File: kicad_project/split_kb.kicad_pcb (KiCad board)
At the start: 2 copper layers, 122 parts, among them J1 Conn_01x03_Pin, J2 Conn_01x04_Socket, J3 4P4C, SW1 B3S-1002

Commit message: Add gitignore (again)
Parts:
- moved H3 135.3 mm to (232.8, 23.8)
- moved J2 62.2 mm to (75.0, 42.7)
- moved J1 35.5 mm to (75.0, 60.5), turned to 180 degrees
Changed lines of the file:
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@@
 	(footprint "MountingHole:MountingHole_3mm_Pad_Via"
 		(layer "F.Cu")
-		(at 216.6 158.05)
+		(at 232.75 23.75)
 		(descr "Mounting Hole 3mm")
 		(tags "mounting hole 3mm")
@@
 	(footprint "Connector_PinHeader_2.54mm:PinHeader_1x04_P2.54mm_Vertical"
 		(layer "F.Cu")
-		(at 26.6 81.7)
+		(at 75.05 42.73)
 		(descr "Through hole straight pin header, 1x04, 2.54mm pitch, single row")
 		(tags "Through hole pin header THT 1x04 2.54mm single row")
@@
 	(footprint "Connector_PinHeader_2.54mm:PinHeader_1x03_P2.54mm_Vertical"
 		(layer "F.Cu")
-		(at 61.769996 93.45 90)
+		(at 75.05 60.49 180)
 		(descr "Through hole straight pin header, 1x03, 2.54mm pitch, single row")
 		(tags "Through hole pin header THT 1x03 2.54mm single row")
 		(property "Reference" "J1"
-			(at 0 -2.33 -90)
+			(at 0 -2.33 180)
 			(layer "F.SilkS")
 			(effects
@@
 		)
 		(property "Value" "Conn_01x03_Pin"
-			(at 0 7.41 -90)
+			(at 0 7.41 180)
 			(layer "F.Fab")
 			(effects
@@
 		)
 		(property "Footprint" "Connector_PinHeader_2.54mm:PinHeader_1x03_P2.54mm_Vertical"
-			(at 0 0 90)
+			(at 0 0 180)
 			(unlocked yes)
 			(layer "F.Fab")
@@
 		)
 		(property "Datasheet" ""
-			(at 0 0 90)
+			(at 0 0 180)
 			(unlocked yes)
 			(layer "F.Fab")
@@
 		)
 		(property "Description" "Generic connector, single row, 01x03, script generated"
-			(at 0 0 90)
+			(at 0 0 180)
 			(unlocked yes)
 			(layer "F.Fab")
@@
 		(attr through_hole)
 		(fp_line
-			(start -1.33 -1.33)
-			(end 0 -1.33)
+			(start 1.33 1.27)
+			(end 1.33 6.41)
 			(stroke
 				(width 0.12)
@@
 		)
 		(fp_line
-			(start -1.33 0)
-			(end -1.33 -1.33)
+			(start -1.33 6.41)
+			(end 1.33 6.41)
 			(stroke
 				(width 0.12)
@@
 		)
 		(fp_line
-			(start 1.33 1.27)
-			(end 1.33 6.41)
+			(start -1.33 1.27)
+			(end 1.33 1.27)
 			(stroke
 				(width 0.12)
@@
 		(fp_line
 			(start -1.33 1.27)
-			(end 1.33 1.27)
+			(end -1.33 6.41)
 			(stroke
 				(width 0.12)
@@
 		)
 		(fp_line
-			(start -1.33 1.27)
-			(end -1.33 6.41)
+			(start -1.33 0)
+			(end -1.33 -1.33)
 			(stroke
 				(width 0.12)
@@
 		)
 		(fp_line
-			(start -1.33 6.41)
-			(end 1.33 6.41)
+			(start -1.33 -1.33)
+			(end 0 -1.33)
 			(stroke
 				(width 0.12)
@@
 		)
 		(fp_line
-			(start 1.8 -1.8)
-			(end -1.8 -1.8)
+			(start 1.8 6.85)
+			(end 1.8 -1.8)
 			(stroke
 				(width 0.05)
@@
 		)
 		(fp_line
-			(start -1.8 -1.8)
-			(end -1.8 6.85)
+			(start 1.8 -1.8)
+			(end -1.8 -1.8)
 			(stroke
 				(width 0.05)
@@
 		)
 		(fp_line
-			(start 1.8 6.85)
-			(end 1.8 -1.8)
+			(start -1.8 6.85)
+			(end 1.8 6.85)
 			(stroke
 				(width 0.05)
@@
 		)
 		(fp_line
-			(start -1.8 6.85)
-			(end 1.8 6.85)
+			(start -1.8 -1.8)
+			(end -1.8 6.85)
 			(stroke
 				(width 0.05)
@@
 		)
 		(fp_line
-			(start 1.27 -1.27)
-			(end 1.27 6.35)
+			(start 1.27 6.35)
+			(end -1.27 6.35)
 			(stroke
 				(width 0.1)
@@
 		)
 		(fp_line
-			(start -0.635 -1.27)
-			(end 1.27 -1.27)
+			(start 1.27 -1.27)
+			(end 1.27 6.35)
 			(stroke
 				(width 0.1)
@@
 		)
 		(fp_line
-			(start -1.27 -0.635)
-			(end -0.635 -1.27)
+			(start -0.635 -1.27)
+			(end 1.27 -1.27)
 			(stroke
 				(width 0.1)
@@
 		)
 		(fp_line
-			(start 1.27 6.35)
-			(end -1.27 6.35)
+			(start -1.27 6.35)
+			(end -1.27 -0.635)
 			(stroke
 				(width 0.1)
@@
 		)
 		(fp_line
-			(start -1.27 6.35)
-			(end -1.27 -0.635)
+			(start -1.27 -0.635)
+			(end -0.635 -1.27)
 			(stroke
 				(width 0.1)
@@
 		)
 		(fp_text user "${REFERENCE}"
-			(at 0 2.54 0)
+			(at 0 2.54 270)
 			(layer "F.Fab")
 			(effects
@@
 		)
 		(pad "1" thru_hole rect
-			(at 0 0 90)
+			(at 0 0 180)
 			(size 1.7 1.7)
 			(drill 1)
@@
 		)
 		(pad "2" thru_hole oval
-			(at 0 2.54 90)
+			(at 0 2.54 180)
 			(size 1.7 1.7)
 			(drill 1)
@@
 		)
 		(pad "3" thru_hole oval
-			(at 0 5.08 90)
+			(at 0 5.08 180)
 			(size 1.7 1.7)
 			(drill 1)

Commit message: Completed first draft of the PCB
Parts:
- removed D_back_1, D_back_10, D_back_11, D_back_12, D_back_13, D_back_14, D_back_15, D_back_16, D_back_17, D_back_18, D_back_19, D_back_2, D_back_20, D_back_21, D_back_22, D_back_23, D_back_24, D_back_25, D_back_26, D_back_27, D_back_28, D_back_3, D_back_4, D_back_5, D_back_6, D_back_7, D_back_8, D_back_9, D_front_1, D_front_10, D_front_11, D_front_12, D_front_13, D_front_14, D_front_15, D_front_16, D_front_17, D_front_18, D_front_19, D_front_2, D_front_20, D_front_21, D_front_22, D_front_23, D_front_24, D_front_25, D_front_26, D_front_27, D_front_28, D_front_3, D_front_4, D_front_5, D_front_6, D_front_7, D_front_8, D_front_9: BAT42W-V, Diode_SMD:D_SOD-123
- removed SW1: B3S-1002, B3S-1002:SW_B3S-1000_OMR
- added D1: 1N5711, Diode_THT:D_DO-35_SOD27_P7.62mm_Horizontal, F.Cu at (84.5, 116.8)
- added D10: 1N5711, Diode_THT:D_DO-35_SOD27_P7.62mm_Horizontal, F.Cu at (184.3, 134.9)
- added D11: 1N5711, Diode_THT:D_DO-35_SOD27_P7.62mm_Horizontal, F.Cu at (172.9, 134.9)
- added D12: 1N5711, Diode_THT:D_DO-35_SOD27_P7.62mm_Horizontal, F.Cu at (161.5, 134.9)
- added D13: 1N5711, Diode_THT:D_DO-35_SOD27_P7.62mm_Horizontal, F.Cu at (84.6, 108.3)
- added D14: 1N5711, Diode_THT:D_DO-35_SOD27_P7.62mm_Horizontal, F.Cu at (84.5, 119.7)
- added D15: 1N5711, Diode_THT:D_DO-35_SOD27_P7.62mm_Horizontal, F.Cu at (84.5, 131.1)
- added D16: 1N5711, Diode_THT:D_DO-35_SOD27_P7.62mm_Horizontal, F.Cu at (198.6, 134.9)
- added D17: 1N5711, Diode_THT:D_DO-35_SOD27_P7.62mm_Horizontal, F.Cu at (187.2, 134.9)
- added D18: 1N5711, Diode_THT:D_DO-35_SOD27_P7.62mm_Horizontal, F.Cu at (175.8, 134.9)
- added D19: 1N5711, Diode_THT:D_DO-35_SOD27_P7.62mm_Horizontal, F.Cu at (164.3, 134.9)
- added D2: 1N5711, Diode_THT:D_DO-35_SOD27_P7.62mm_Horizontal, F.Cu at (204.2, 134.9)
- added D20: 1N5711, Diode_THT:D_DO-35_SOD27_P7.62mm_Horizontal, F.Cu at (84.5, 111.2)
- added D21: 1N5711, Diode_THT:D_DO-35_SOD27_P7.62mm_Horizontal, F.Cu at (84.5, 122.5)
- added D22: 1N5711, Diode_THT:D_DO-35_SOD27_P7.62mm_Horizontal, F.Cu at (84.5, 128.2)
- added D23: 1N5711, Diode_THT:D_DO-35_SOD27_P7.62mm_Horizontal, F.Cu at (201.4, 134.9)
- added D24: 1N5711, Diode_THT:D_DO-35_SOD27_P7.62mm_Horizontal, F.Cu at (190.0, 134.9)
- added D25: 1N5711, Diode_THT:D_DO-35_SOD27_P7.62mm_Horizontal, F.Cu at (178.6, 134.9)
- added D26: 1N5711, Diode_THT:D_DO-35_SOD27_P7.62mm_Horizontal, F.Cu at (167.2, 134.9)
- added D27: 1N5711, Diode_THT:D_DO-35_SOD27_P7.62mm_Horizontal, F.Cu at (84.5, 102.6)
- added D28: 1N5711, Diode_THT:D_DO-35_SOD27_P7.62mm_Horizontal, F.Cu at (84.5, 125.4)
- added D3: 1N5711, Diode_THT:D_DO-35_SOD27_P7.62mm_Horizontal, F.Cu at (192.8, 134.9)
- added D4: 1N5711, Diode_THT:D_DO-35_SOD27_P7.62mm_Horizontal, F.Cu at (181.4, 134.9)
- added D5: 1N5711, Diode_THT:D_DO-35_SOD27_P7.62mm_Horizontal, F.Cu at (170.1, 134.9)
- added D6: 1N5711, Diode_THT:D_DO-35_SOD27_P7.62mm_Horizontal, F.Cu at (84.5, 105.5)
- added D7: 1N5711, Diode_THT:D_DO-35_SOD27_P7.62mm_Horizontal, F.Cu at (84.5, 114.0)
- added D8: 1N5711, Diode_THT:D_DO-35_SOD27_P7.62mm_Horizontal, F.Cu at (84.5, 133.9)
- added D9: 1N5711, Diode_THT:D_DO-35_SOD27_P7.62mm_Horizontal, F.Cu at (195.7, 134.9)
- added H5: MountingHole, MountingHole:MountingHole_3mm_Pad_Via, F.Cu at (73.2, 123.5)
- added J4: Conn_01x04_Pin, Connector_PinHeader_2.54mm:PinHeader_1x04_P2.54mm_Vertical, F.Cu at (69.3, 72.8)
- added R0: R, Resistor_THT:R_Axial_DIN0204_L3.6mm_D1.6mm_P5.08mm_Horizontal, F.Cu at (77.9, 79.8)
- added R1: R, Resistor_THT:R_Axial_DIN0204_L3.6mm_D1.6mm_P5.08mm_Horizontal, F.Cu at (80.8, 79.8)
- added R2: R, Resistor_THT:R_Axial_DIN0204_L3.6mm_D1.6mm_P5.08mm_Horizontal, F.Cu at (83.6, 79.8)
- added R3: R, Resistor_THT:R_Axial_DIN0204_L3.6mm_D1.6mm_P5.08mm_Horizontal, F.Cu at (86.5, 79.8)
- J1: value Conn_01x03_Pin -> 4P4C; footprint Connector_PinHeader_2.54mm:PinHeader_1x03_P2.54mm_Vertical -> Connector_RJ:RJ9_Evercom_5301-440xxx_Horizontal; moved to B.Cu
- moved H1 125.5 mm to (73.2, 95.0)
- moved H2 99.3 mm to (96.9, 162.4)
- moved H4 33.7 mm to (230.8, 133.9)
- moved J2 26.3 mm to (69.3, 68.4), turned to 180 degrees
- moved J3 20.4 mm to (82.6, 53.9)
- moved U_front1 20.0 mm to (99.8, 57.0)
- moved U_back1 20.0 mm to (96.0, 57.0)
- moved H3 20.0 mm to (231.8, 43.7)
- moved SW_back_8 19.6 mm to (108.0, 146.3)
- moved SW_front_8 19.6 mm to (108.0, 146.3)
- moved SW_back_15 19.6 mm to (124.5, 136.8)
- moved SW_front_15 19.6 mm to (124.5, 136.8)
- moved SW_back_12 19.6 mm to (166.2, 68.4)
- moved SW_front_12 19.6 mm to (166.2, 68.4)
- moved SW_back_1 19.6 mm to (109.2, 104.5)
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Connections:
- J1 pad 1: VCC -> GND
- J1 pad 2: EN_JUMP -> UART_TX
- J1 pad 3: GND -> UART_RX
- U_back1 pad 1: UART_TX -> UART_RX
- U_back1 pad 2: UART_RX -> UART_TX
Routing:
- net Net-(D15-K): track 0.00 -> 213.5 mm
- net Net-(D10-K): track 0.00 -> 190.0 mm
- net Net-(D1-K): track 0.00 -> 187.2 mm, vias 0 -> 1
- net Net-(D22-K): track 0.00 -> 184.0 mm
- net Net-(D7-A): track 24.4 -> 127.6 mm, vias 0 -> 1
- net Net-(D14-A): track 0.00 -> 97.0 mm, vias 0 -> 1
- net Net-(D21-A): track 0.00 -> 97.0 mm, vias 0 -> 1
- net Net-(D20-A): track 74.8 -> 167.0 mm
- net Net-(D13-A): track 65.1 -> 156.0 mm
- net COL_1: track 202.2 -> 292.6 mm, vias 5 -> 4
- net Net-(D27-A): track 118.3 -> 207.9 mm
- net Net-(D6-A): track 57.3 -> 146.0 mm, vias 1 -> 3
- net EN_JUMP: track 0.00 -> 80.5 mm, vias 0 -> 2
- net COL_2: track 183.0 -> 263.3 mm, vias 5 -> 4
- net Net-(D22-A): track 0.00 -> 77.5 mm, vias 0 -> 1
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- added copper zone on B.Cu, net GND
- added copper zone on F.Cu, net GND
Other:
- board outline added: 171 x 130 mm

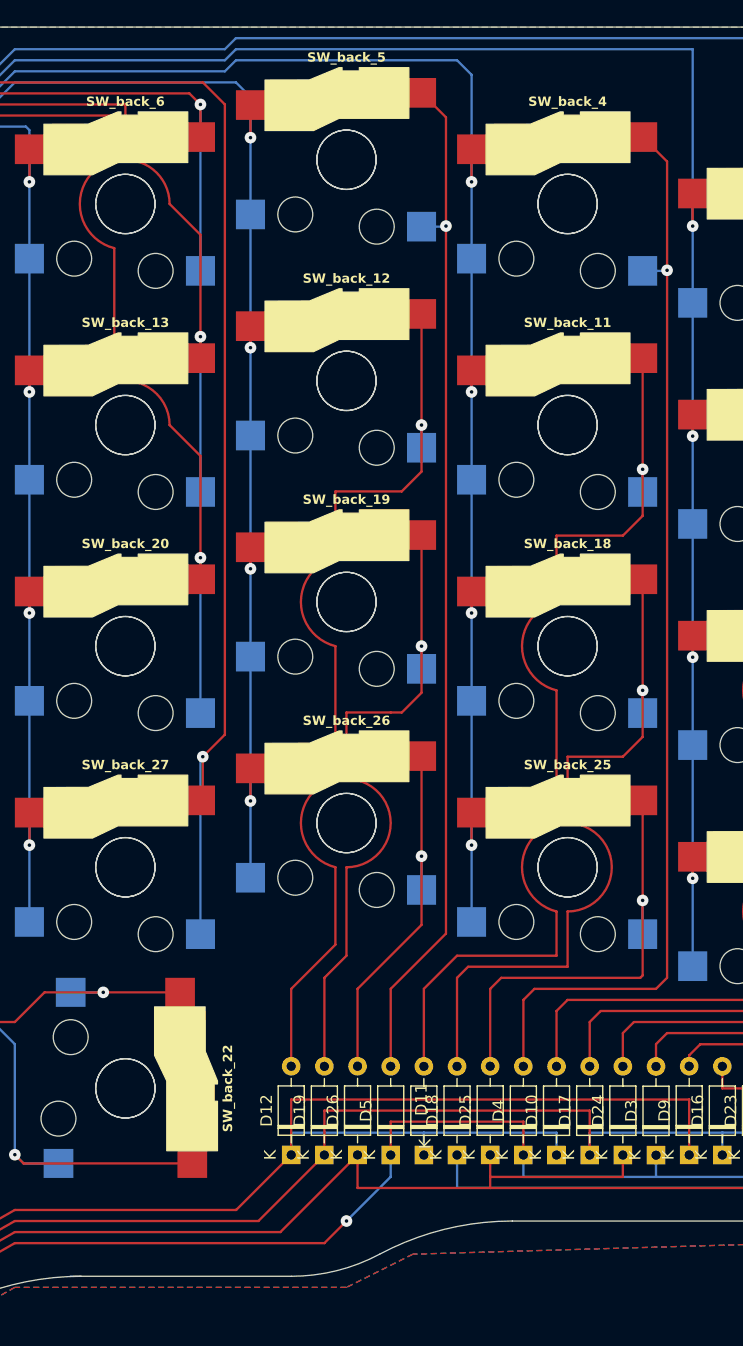
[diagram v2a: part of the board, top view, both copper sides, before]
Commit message: Fixed edge cut error, changed vertical stagging a bit
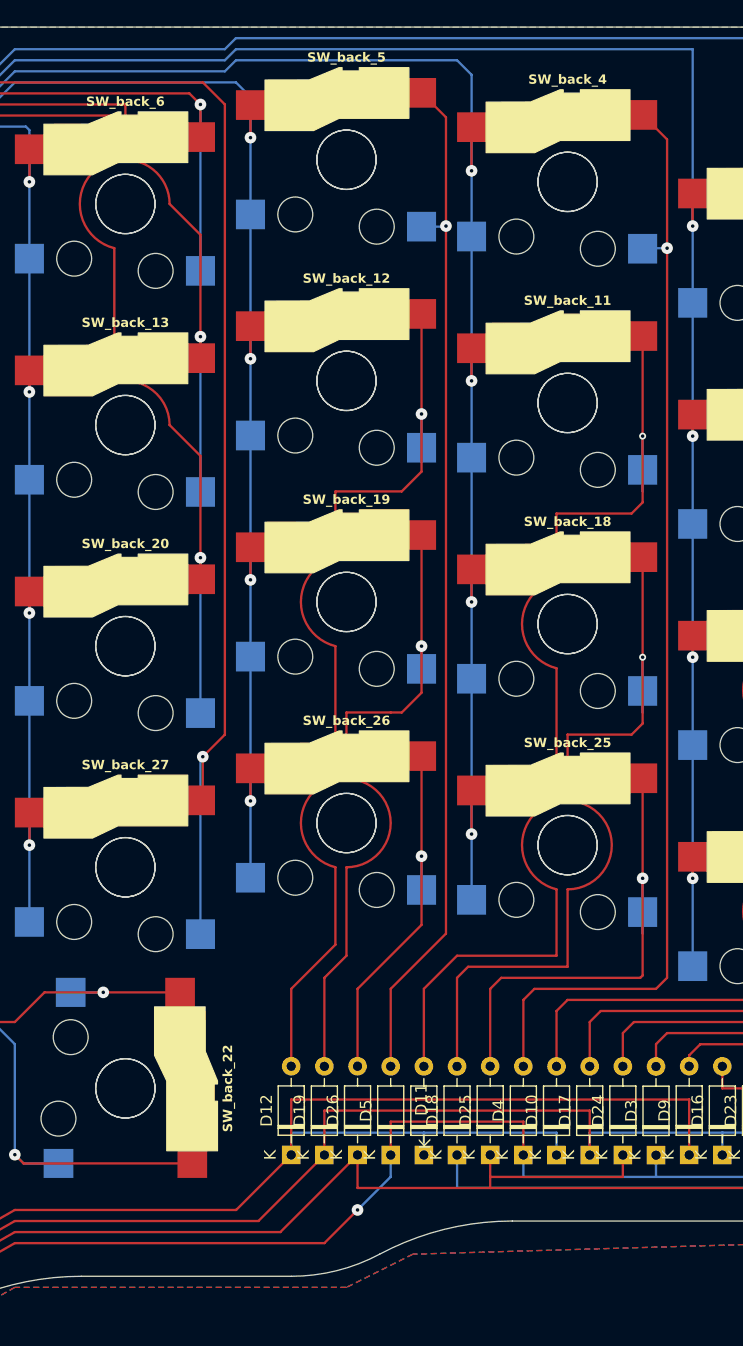
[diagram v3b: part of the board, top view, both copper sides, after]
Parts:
- moved SW_back_11 1.90 mm to (185.2, 70.3)
- moved SW_back_18 1.90 mm to (185.2, 89.3)
- moved SW_back_25 1.90 mm to (185.2, 108.3)
- moved SW_back_4 1.90 mm to (185.2, 51.3)
- moved SW_front_11 1.90 mm to (185.2, 70.3)
- moved SW_front_18 1.90 mm to (185.2, 89.3)
- moved SW_front_25 1.90 mm to (185.2, 108.3)
- moved SW_front_4 1.90 mm to (185.2, 51.3)
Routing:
- net Net-(D18-A): track 50.6 -> 55.8 mm
- net Net-(D11-A): track 63.7 -> 69.0 mm
- net Net-(D25-A): track 38.2 -> 42.0 mm
- net COL_3: track 231.0 -> 232.9 mm
- net Net-(D4-A): track 94.1 -> 96.0 mm
- net COL_4: track 196.8 -> 198.7 mm
- net Net-(D12-A): track 59.4 -> 60.3 mm
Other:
- outline, holes or cut-outs redrawn

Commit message: Moved one of the holes up
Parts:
- moved H1 80.7 mm to (128.2, 36.1)
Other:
- board size 171 x 130 mm -> 171 x 137.6 mm
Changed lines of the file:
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@@
 	(footprint "MountingHole:MountingHole_3mm_Pad_Via"
 		(layer "F.Cu")
-		(at 73.15 95)
+		(at 128.25 36.1)
 		(descr "Mounting Hole 3mm")
 		(tags "mounting hole 3mm")
@@
 	)
 	(gr_line
+		(start 135.85 38)
+		(end 231.8 38)
+		(stroke
+			(width 0.05)
+			(type default)
+		)
+		(layer "Edge.Cuts")
+	)
+	(gr_line
 		(start 180.5 140.6)
 		(end 231.8 140.6)
@@
 		(layer "Edge.Cuts")
 	)
+	(gr_arc
+		(start 122.55 36.1)
+		(mid 128.25 30.4)
+		(end 133.95 36.1)
+		(stroke
+			(width 0.05)
+			(type default)
+		)
+		(layer "Edge.Cuts")
+	)
 	(gr_line
 		(start 143.45 145.35)
@@
 		(layer "Edge.Cuts")
 	)
+	(gr_arc
+		(start 135.85 38)
+		(mid 134.506497 37.443503)
+		(end 133.95 36.1)
+		(stroke
+			(width 0.05)
+			(type default)
+		)
+		(layer "Edge.Cuts")
+	)
+	(gr_arc
+		(start 122.55 36.1)
+		(mid 121.993503 37.443503)
+		(end 120.65 38)
+		(stroke
+			(width 0.05)
+			(type default)
+		)
+		(layer "Edge.Cuts")
+	)
 	(gr_line
 		(start 66.5 38)
-		(end 231.8 38)
+		(end 120.65 38)
 		(stroke
 			(width 0.05)
@@
 		(polygon
 			(pts
-				(xy 66.5 38) (xy 237.5 38) (xy 237.5 141.55) (xy 171.95 143.45) (xy 166.25 146.3) (xy 137.75 146.3)
+				(xy 66.5 27.55) (xy 237.5 28.5) (xy 237.5 141.55) (xy 171.95 143.45) (xy 166.25 146.3) (xy 137.75 146.3)
 				(xy 94.05 171) (xy 66.5 126.35)
 			)
@@
 		(polygon
 			(pts
-				(xy 66.5 38) (xy 237.5 38) (xy 237.5 141.55) (xy 171.95 143.45) (xy 166.25 146.3) (xy 137.75 146.3)
+				(xy 66.5 27.55) (xy 237.5 28.5) (xy 237.5 141.55) (xy 171.95 143.45) (xy 166.25 146.3) (xy 137.75 146.3)
 				(xy 94.05 171) (xy 66.5 126.35)
 			)
